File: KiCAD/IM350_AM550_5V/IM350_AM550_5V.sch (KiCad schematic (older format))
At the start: 10 parts, among them J5 USB_B_Micro_Power, J7 RJ12, P3 0R, P4 0R, SW1 Pairing, U1 MCP1700-3302E_SOT23, U2 ESP-12F

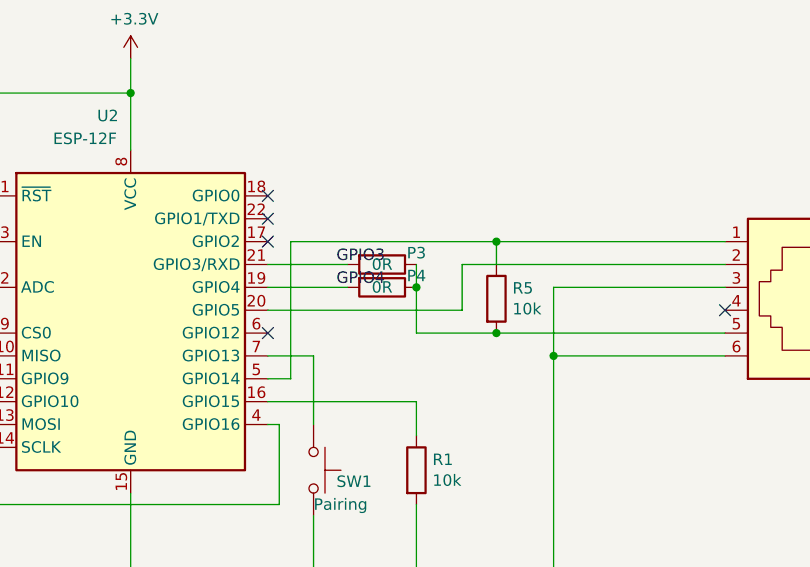
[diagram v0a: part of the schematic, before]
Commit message: Website handleSettings bugfix
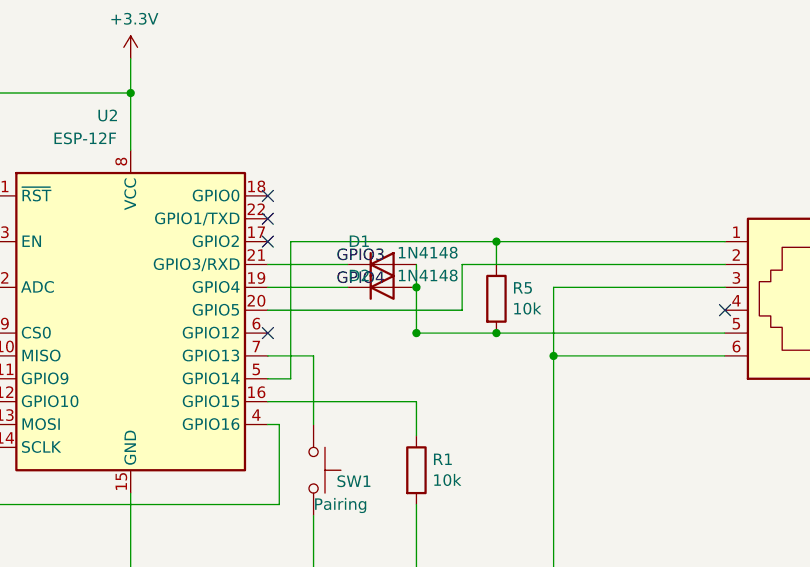
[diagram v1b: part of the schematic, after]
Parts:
- removed P3, P4: 0R, Resistor_SMD:R_0402_1005Metric_Pad0.72x0.64mm_HandSolder, symbol Device:R
- added D1, D2: 1N4148, Diode_SMD:D_0805_2012Metric_Pad1.15x1.40mm_HandSolder, symbol Diode:1N4148
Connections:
- net GPIO3: now also D1.1 (K)
- net GPIO4: now also D2.1 (K)
- net at J7.5, R5.2: now also D1.2 (A), D2.2 (A)
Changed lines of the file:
@@
 NoConn ~ 5450 3000
 NoConn ~ 5450 3100
-$Comp
-L Device:R P3
-U 1 1 606C9BA3
-P 7150 2300
-F 0 "P3" V 7100 2450 50  0000 C CNN
-F 1 "0R" V 7150 2300 50  0000 C CNN
-F 2 "Resistor_SMD:R_0402_1005Metric_Pad0.72x0.64mm_HandSolder" V 7080 2300 50  0001 C CNN
-F 3 "~" H 7150 2300 50  0001 C CNN
-	1    7150 2300
-	0    1    1    0
-$EndComp
 Connection ~ 7650 2600
 Wire Wire Line
@@
 	6650 2500 7500 2500
 Wire Wire Line
-	7300 2300 7300 2400
-Wire Wire Line
 	7300 2600 7650 2600
 Wire Wire Line
@@
 Wire Wire Line
 	3500 2500 4200 2500
-$Comp
-L Device:R P4
-U 1 1 60715416
-P 7150 2400
-F 0 "P4" V 7100 2550 50  0000 C CNN
-F 1 "0R" V 7150 2400 50  0000 C CNN
-F 2 "Resistor_SMD:R_0402_1005Metric_Pad0.72x0.64mm_HandSolder" V 7080 2400 50  0001 C CNN
-F 3 "~" H 7150 2400 50  0001 C CNN
-	1    7150 2400
-	0    1    1    0
-$EndComp
-Connection ~ 7300 2400
-Wire Wire Line
-	7300 2400 7300 2600
 Wire Wire Line
 	6650 2400 7000 2400
@@
 NoConn ~ 6650 2000
 NoConn ~ 6650 2100
+$Comp
+L Diode:1N4148 D1
+U 1 1 610C3121
+P 7150 2300
+F 0 "D1" H 7050 2400 50  0000 C CNN
+F 1 "1N4148" H 7350 2350 50  0000 C CNN
+F 2 "Diode_SMD:D_0805_2012Metric_Pad1.15x1.40mm_HandSolder" H 7150 2125 50  0001 C CNN
+F 3 "https://assets.nexperia.com/documents/data-sheet/1N4148_1N4448.pdf" H 7150 2300 50  0001 C CNN
+	1    7150 2300
+	1    0    0    -1
+$EndComp
+Wire Wire Line
+	7300 2300 7300 2400
+$Comp
+L Diode:1N4148 D2
+U 1 1 610C5275
+P 7150 2400
+F 0 "D2" H 7050 2450 50  0000 C CNN
+F 1 "1N4148" H 7350 2450 50  0000 C CNN
+F 2 "Diode_SMD:D_0805_2012Metric_Pad1.15x1.40mm_HandSolder" H 7150 2225 50  0001 C CNN
+F 3 "https://assets.nexperia.com/documents/data-sheet/1N4148_1N4448.pdf" H 7150 2400 50  0001 C CNN
+	1    7150 2400
+	1    0    0    -1
+$EndComp
+Connection ~ 7300 2400
+Wire Wire Line
+	7300 2400 7300 2600
+Connection ~ 7300 2600
 $EndSCHEMATC
